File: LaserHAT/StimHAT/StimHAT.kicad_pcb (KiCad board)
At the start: 4 copper layers, 65 x 57 mm, 112 parts, among them J1 GPIO, J10 OLED 0.91 (GND VCC SCL SDA), J101 ELECTRODE E1/E2, J102 B4B-PH-K-S(LF)(SN), J103 5V TO DC-DC POD, J5 GT-USB-7010ASV, J6 BNC TRIGGER IN, J7 BNC STIM OUT, Q3 AP30P30Q, Q4 DMMT5401, Q5 AP30P30Q, SW10 MSK12C02, SW6 TS-1088-AR02016, SW7 SKRHADE010, SW9 TS-1088-AR02016, U1 M24C32-WDW6TP, U101 ISO7741FDBQR, U104 TLV76050DBZR, U105 DAC60501ZDGSR, U106 OPA2192IDGKR, U107 CD74HC4053PWR, U108 DG418DY-T1-E3, U109 ISO1640BDR, U110 TLV1702AIDGKR, U4 MCP1700T-3302E/MB, U5 AP2171W, U6 CH340N, U7 MSPM0G1507SRHBR, U8 74LVC2G17GW

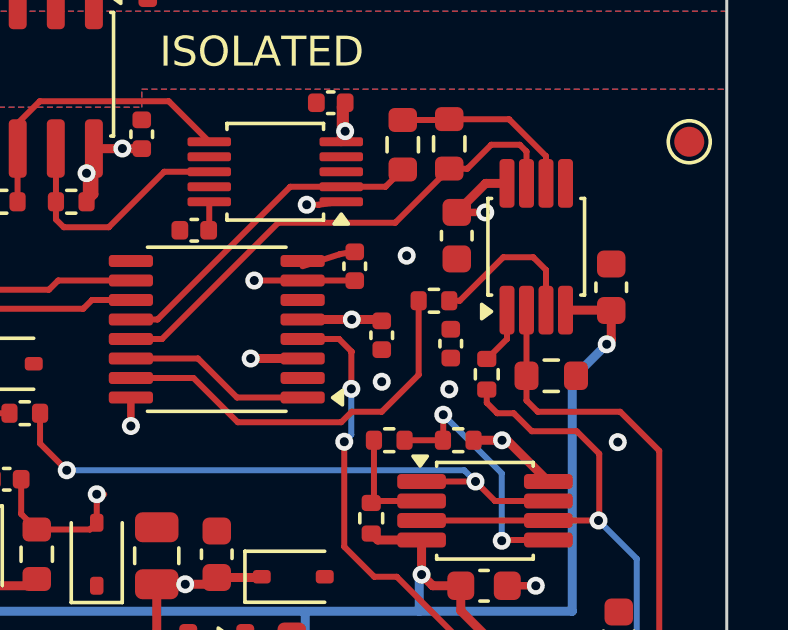
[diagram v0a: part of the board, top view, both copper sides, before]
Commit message: Cleaned up routing in isolated segment again
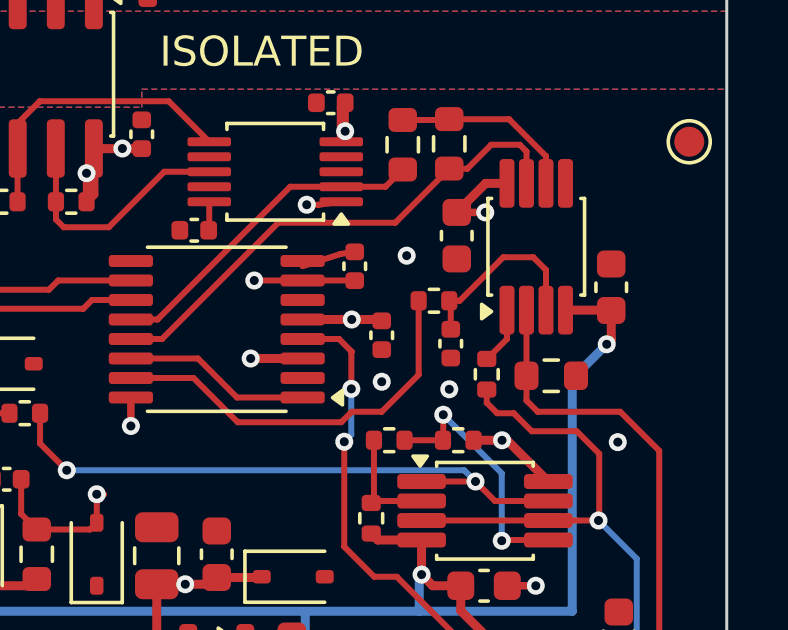
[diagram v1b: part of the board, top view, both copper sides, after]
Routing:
- net OA_IN: track 5.34 -> 6.31 mm
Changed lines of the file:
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@@
+	)
+	(segment
+		(start 55.8 27.1)
+		(end 55.75 27.05)
+		(width 0.2)
+		(layer "F.Cu")
+		(net 106)
 	)
 	(segment
@@
 		(width 0.2)
 		(layer "F.Cu")
+		(net 106)
+	)
+	(segment
+		(start 55.8 28)
+		(end 55.8 27.1)
+		(width 0.2)
+		(layer "F.Cu")
